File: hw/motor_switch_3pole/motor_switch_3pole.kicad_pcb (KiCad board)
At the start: 2 copper layers, 54 x 54 mm, 24 parts, among them J1 CONN_3X1, J2 CONN_2X1, J3 CONN_6X1, Q1 BSS138, Q2 BSS138

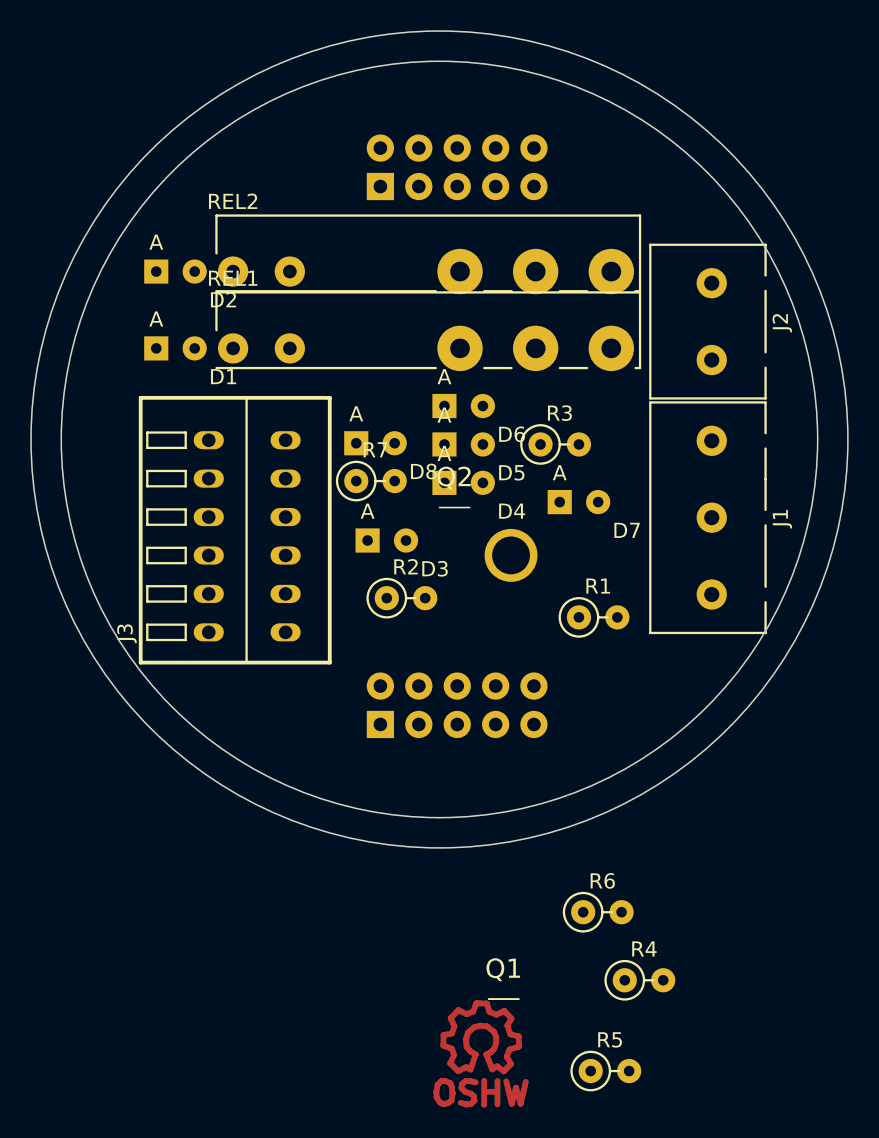
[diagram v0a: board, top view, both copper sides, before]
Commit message: changed to SMD components
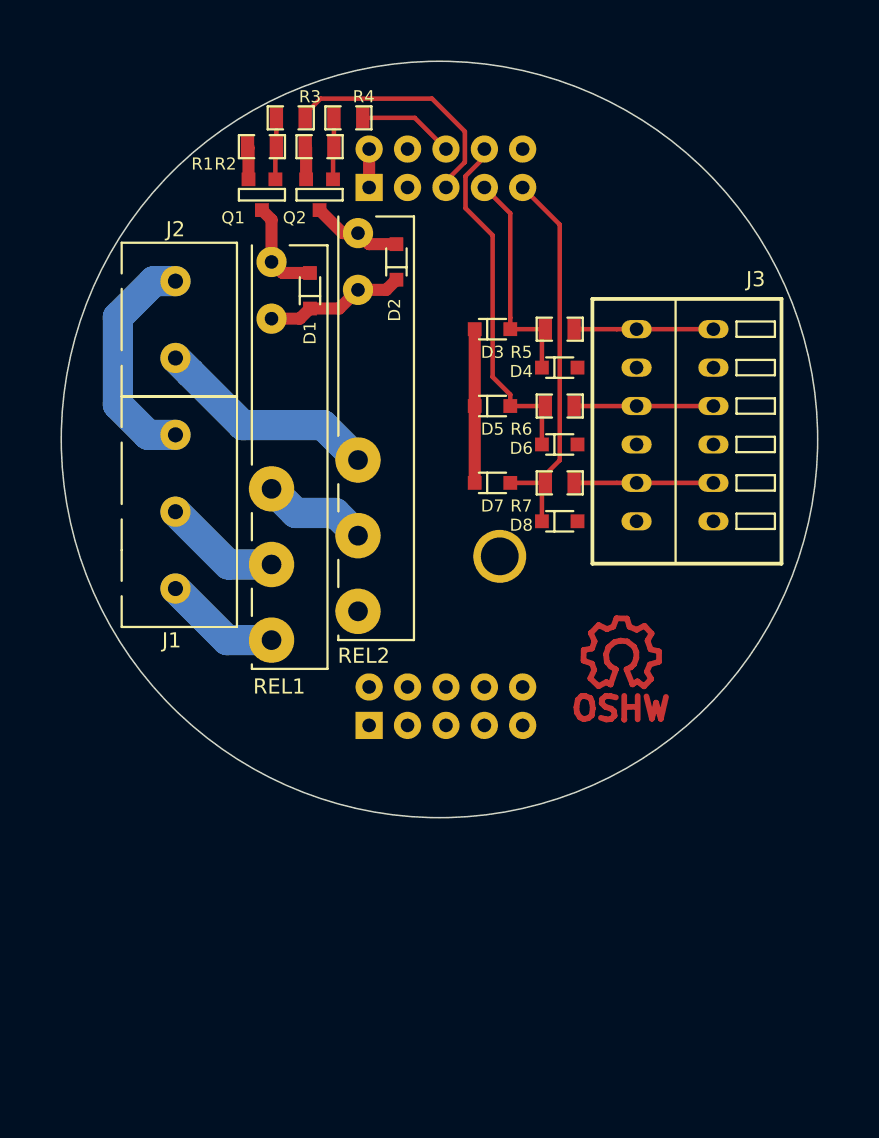
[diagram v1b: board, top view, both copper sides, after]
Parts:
- D1, D2, D3, D4, D5, D6, D7, D8: footprint Diode_THT:D_RM2.54mm -> Diode_SMD:D_SOD323
- R1, R2, R3, R4, R5, R6, R7: footprint Resistor:R_RM2.54mm -> Resistor:R_0805
- moved R4 59.9 mm to (94.0, 78.7)
- moved Q1 55.5 mm to (88.3, 83.8)
- moved R5 49.1 mm to (108.0, 92.7)
- moved J3 38.9 mm to (118.1, 92.7), turned to 270 degrees
- moved R1 37.5 mm to (88.3, 80.6), turned to 180 degrees
- moved J1 37.0 mm to (82.5, 99.7), turned to 270 degrees
- moved J2 35.8 mm to (82.5, 89.5), turned to 270 degrees
- moved R6 33.5 mm to (108.0, 97.8)
- moved R2 30.2 mm to (92.1, 80.6), turned to 180 degrees
- moved R3 27.2 mm to (90.2, 78.7)
- moved LOGO1 27.1 mm to (112.0, 114.3)
- moved Q2 22.5 mm to (92.1, 83.8)
- moved D3 16.2 mm to (103.5, 92.7), turned to 180 degrees
- moved D2 15.9 mm to (97.2, 88.3), turned to 270 degrees
- moved D8 14.4 mm to (108.0, 105.4), turned to 180 degrees
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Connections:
- net Net-(REL1-Pad3) renamed /230V_ON
- D7 pad 1: //button_close -> //switch_close
- D8 pad 2: //button_close -> //switch_close
- J1 pad 1: Net-(J1-Pad1) -> /230V_N
- J1 pad 2: Net-(J1-Pad2) -> /230V_UP
- J1 pad 3: Net-(J1-Pad3) -> /230V_DOWN
- J2 pad 1: Net-(J2-Pad1) -> /230V_N
- J2 pad 2: Net-(J1-Pad2) -> /230V_L
- MOD1 pad 9: (no net) -> //switch_close
- R7 pad 1: //button_close -> //switch_close
- REL1 pad 4: Net-(J1-Pad3) -> /230V_UP
- REL1 pad 5: Net-(J1-Pad1) -> /230V_DOWN
- REL2 pad 3: Net-(J2-Pad1) -> /230V_L
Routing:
- net //switch_close: track 0.00 -> 25.9 mm
- net //button_down: track 0.00 -> 23.7 mm
- net /relay_up_down: track 0.00 -> 16.3 mm
- net /230V_N: track 0.00 -> 15.2 mm
- net //button_up: track 0.00 -> 15.0 mm
- net /230V_L: track 0.00 -> 14.9 mm
- net +5V: track 0.00 -> 10.2 mm
- net +24V: track 0.00 -> 9.32 mm
- net Net-(J3-Pad5): track 0.00 -> 9.21 mm
- net Net-(J3-Pad3): track 0.00 -> 9.21 mm
- net Net-(J3-Pad1): track 0.00 -> 9.21 mm
- net /230V_UP: track 0.00 -> 7.80 mm
- net /230V_DOWN: track 0.00 -> 7.76 mm
- net /230V_ON: track 0.00 -> 7.00 mm
- net GND: track 0.00 -> 6.91 mm
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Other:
- board size 54 x 54 mm -> 50 x 50 mm
- net class 230V added: clearance 1.5, trace_width 2, via_dia 2.5, via_drill 0.8
- net class Default: trace_width 0.25 -> 0.3; via_dia 0.6 -> 0.8
- net class Power added: clearance 0.4, trace_width 0.8, via_dia 1, via_drill 0.5

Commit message: motor control 3pole layouted and ready for review
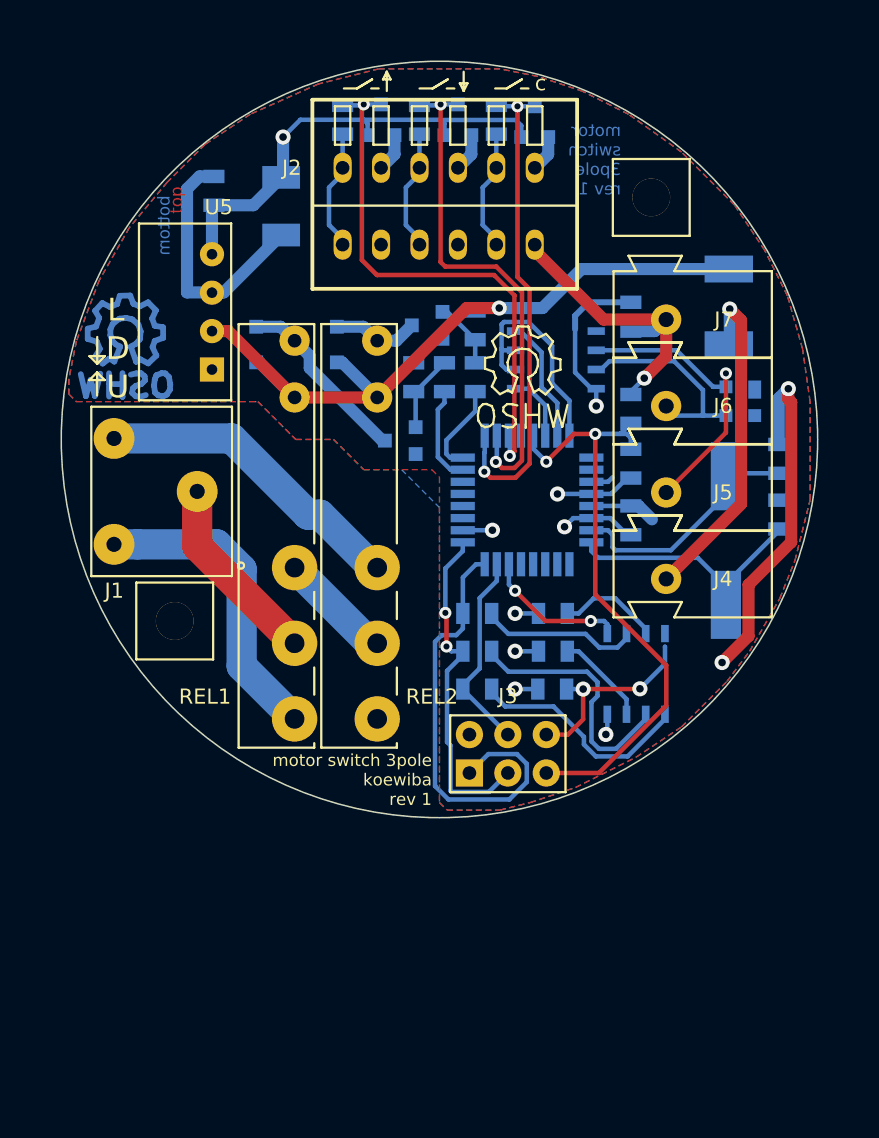
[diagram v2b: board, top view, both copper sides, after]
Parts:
- removed D7, D8: 1N4148, Diode_SMD:D_SOD323
- removed MOD1: bus-module_attiny1634, Modules:bus-module_attiny1634
- added C1: 100nF, Capacitors_SMD:C_0805, B.Cu at (112.6, 105.3)
- added C2: 100nF, Capacitors_SMD:C_0805, B.Cu at (107.5, 116.5)
- added C4: 18pF, Capacitors_SMD:C_0805, B.Cu at (122.4, 101.3)
- added C5: 18pF, Capacitors_SMD:C_0805, B.Cu at (122.4, 105.0)
- added C6: 4,7nF, Capacitors_SMD:C_0805, B.Cu at (112.6, 98.0)
- added C7: 47µF / 4V, Capacitors_SMD:C_0805, B.Cu at (85.1, 83.6)
- added C8: 100nF, Capacitors_SMD:C_0805, B.Cu at (112.6, 91.9)
- added D10: SEMTECH SR05, Diode_SMD:D_SOT143, B.Cu at (119.9, 97.5)
- added F1: FUSE, Resistor:R_1812, B.Cu at (119.1, 91.2)
- added H1: HOLE, Mechanical:HOLE_2.5mm_wo_Copper, F.Cu at (114.0, 84.0)
- added H2: HOLE, Mechanical:HOLE_2.5mm_wo_Copper, F.Cu at (82.5, 112.0)
- added J4: CONN_1, Connector_WAGO:WAGO_243, F.Cu at (111.5, 111.8)
- added J5: CONN_1, Connector_WAGO:WAGO_243, F.Cu at (111.5, 106.0)
- added J6: CONN_1, Connector_WAGO:WAGO_243, F.Cu at (111.5, 100.3)
- added J7: CONN_1, Connector_WAGO:WAGO_243, F.Cu at (111.5, 94.6)
- added LOGO2: Open Hardware, Symbol:Symbol_OSHW-Logo_SilkScreen, F.Cu at (105.5, 95.0)
- added R10: 100, Resistor:R_0805, B.Cu at (102.5, 116.5)
- added R11: 100, Resistor:R_0805, B.Cu at (102.5, 114.0)
- added R12: 10k, Resistor:R_0805, B.Cu at (107.5, 114.0)
- added R13: 10k, Resistor:R_0805, B.Cu at (112.6, 101.6)
- added R8: 10k, Resistor:R_0805, B.Cu at (107.5, 111.5)
- added R9: 100, Resistor:R_0805, B.Cu at (102.5, 111.5)
- added U1: 25LC256, Housings_SOIC:SO8E, B.Cu at (113.0, 115.5)
- added U2: ATMEGA328-TQFP32, Housings_QFP:TQFP-32_7x7mm_Pitch0.8mm, B.Cu at (105.8, 104.0)
- added U3: 7,3728MHz, Crystal:CRY_HC49_SMD, B.Cu at (118.9, 106.7)
- added U4: MAX487ECSA, Housings_SOIC:SO8E, B.Cu at (107.7, 94.7)
- added U5: AM1S-2403, DCDC_Converter:AM1S-XXXX_SIL4, F.Cu at (85.0, 95.4)
- D1, D2, LOGO1, Q1, Q2, R1, R2, R3, R4: moved to B.Cu
- D3: value 1N4148 -> ZD5V6; footprint Diode_SMD:D_SOD323 -> Diode_SMD:D_MINIMELF; moved to B.Cu
- D4, D5, D6: value 1N4148 -> BAT54S; footprint Diode_SMD:D_SOD323 -> Housings_SOT:SOT23-3; moved to B.Cu
- J1: footprint Connector_Miscelleaneus:CLAMP_5,08mm_3pole_stackable -> Connector_WAGO:WAGO_2081-1123
- J2: value CONN_2X1 -> CONN_6X1; footprint Connector_Miscelleaneus:CLAMP_5,08mm_2pole_stackable -> Connector_WAGO:WAGO_233-6
- J3: value CONN_6X1 -> CONN-ISP-6; footprint Connector_Miscelleaneus:WAGO_233-6 -> Connector_Header:HEADER_3x2
- R5, R6, R7: value 1k -> 4k7; moved to B.Cu
- moved LOGO1 39.1 mm to (79.2, 93.0), turned to 180 degrees
- moved J3 33.5 mm to (102.0, 122.0), turned to 0 degrees
- moved R7 24.4 mm to (103.8, 78.9), turned to 270 degrees
- moved D6 21.4 mm to (106.3, 79.0), turned to 0 degrees
- moved R6 21.1 mm to (98.7, 78.9), turned to 270 degrees
- moved D4 20.2 mm to (96.1, 78.9), turned to 0 degrees
- moved R5 19.9 mm to (93.6, 78.9), turned to 270 degrees
- moved R3 19.9 mm to (100.3, 95.9), turned to 270 degrees
- moved R4 19.1 mm to (102.4, 95.9), turned to 270 degrees
- moved D5 19.1 mm to (101.2, 78.9), turned to 0 degrees
- moved Q1 18.7 mm to (97.4, 100.1), turned to 90 degrees
- moved R1 18.2 mm to (98.3, 95.9), turned to 90 degrees
- moved D3 16.2 mm to (89.5, 84.6), turned to 90 degrees
- moved R2 15.7 mm to (102.4, 92.5), turned to 90 degrees
- moved J2 13.4 mm to (93.6, 82.0), turned to 0 degrees
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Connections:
- D3 pad 1: //button_up -> GND
- D4 pad 2: //button_up -> +5V
- D5 pad 1: //button_down -> GND
- D6 pad 2: //button_down -> +5V
- J1 pad 1: /230V_N -> /230V_UP
- J1 pad 2: /230V_UP -> /230V_DOWN
- J1 pad 3: /230V_DOWN -> /230V_L
- J2 pad 1: /230V_N -> Net-(J2-Pad1)
- J2 pad 2: /230V_L -> GND
- J3 pad 1: Net-(J3-Pad1) -> /bus_atmega328_basic/PB4_MISO
- J3 pad 2: GND -> +5V
- J3 pad 3: Net-(J3-Pad3) -> /bus_atmega328_basic/PB5_SCK
- J3 pad 4: GND -> /bus_atmega328_basic/PB3_MOSI
- J3 pad 5: Net-(J3-Pad5) -> /bus_atmega328_basic//RESET
- R5 pad 2: Net-(J3-Pad1) -> Net-(J2-Pad1)
- R6 pad 2: Net-(J3-Pad3) -> Net-(J2-Pad3)
- R7 pad 2: Net-(J3-Pad5) -> Net-(J2-Pad5)
- REL1 pad 4: /230V_UP -> /230V_DOWN
- REL1 pad 5: /230V_DOWN -> /230V_UP
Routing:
- net GND: track 6.91 -> 87.7 mm, vias 0 -> 5
- net +5V: track 10.2 -> 59.7 mm, vias 0 -> 9
- net /bus_atmega328_basic//RESET: track 0.00 -> 40.0 mm, vias 0 -> 2
- net +24V: track 9.32 -> 46.7 mm, vias 0 -> 1
- net /bus_atmega328_basic/PB4_MISO: track 0.00 -> 29.6 mm
- net /bus_atmega328_basic/PB5_SCK: track 0.00 -> 22.7 mm, vias 0 -> 2
- net Net-(F1-Pad2): track 0.00 -> 22.6 mm, vias 0 -> 1
- net //button_up: track 15.0 -> 36.1 mm, vias 0 -> 2
- net /bus_atmega328_basic/A: track 0.00 -> 19.8 mm, vias 0 -> 1
- net Net-(C5-Pad1): track 0.00 -> 18.8 mm
- net Net-(C4-Pad1): track 0.00 -> 17.7 mm
- net /bus_atmega328_basic/SCK: track 0.00 -> 17.0 mm
- net /bus_atmega328_basic/TXD0EN: track 0.00 -> 15.3 mm
- net /230V_N: track 15.2 -> 0.00 mm
- net /bus_atmega328_basic/MOSI: track 0.00 -> 15.1 mm
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- added copper zone on F.Cu, net +5V
- added copper zone on B.Cu, net GND
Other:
- net class 230V: clearance 1.5 -> 1
- net class Power: clearance 0.4 -> 0.2
- board text added: "D"
- board text added: "L"
- board text added: "U"
- board text added: "bottom"
- board text added: "c"
- board text added: "motor switch 3pole koewiba rev 1"
- board text added: "motor switch 3pole rev 1"
- board text added: "top"

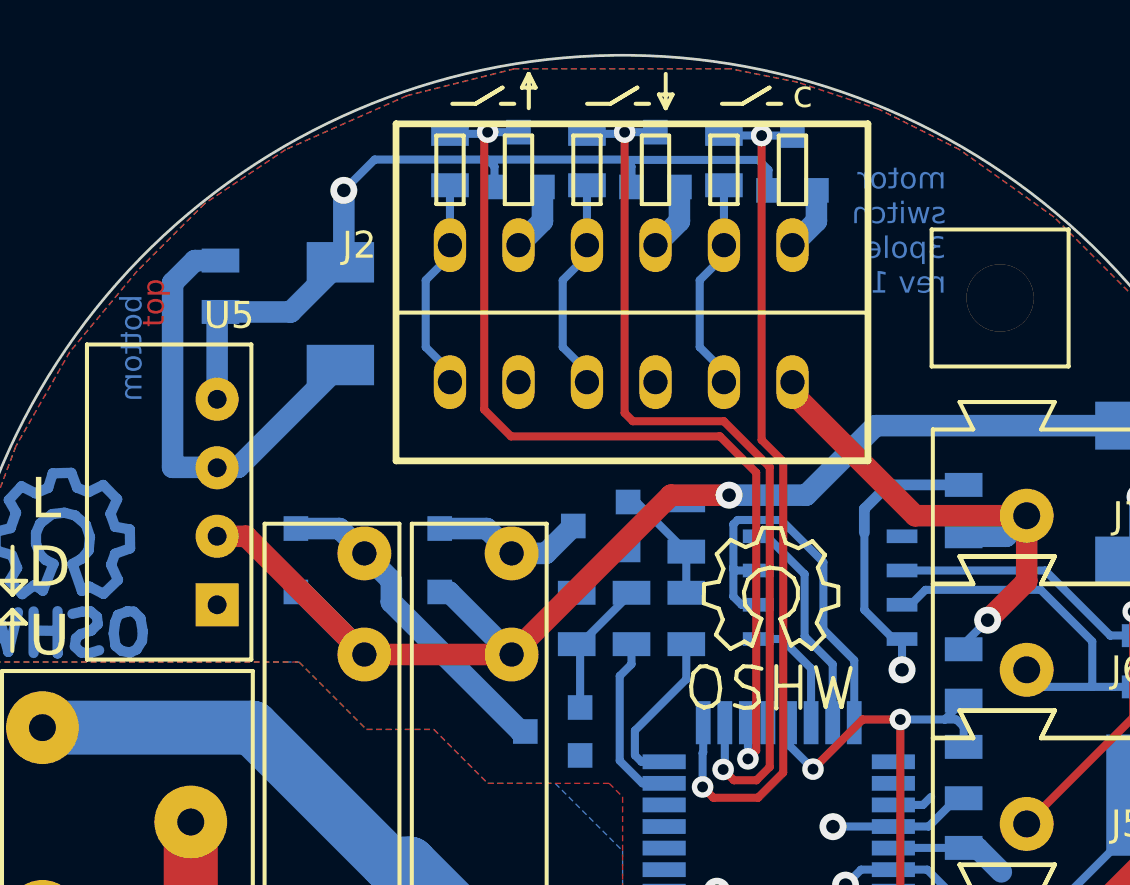
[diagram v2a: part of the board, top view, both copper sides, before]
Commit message: Final revision 1 files of motor_switch_3pole added. Prototype PCBs of this revision have been ordered
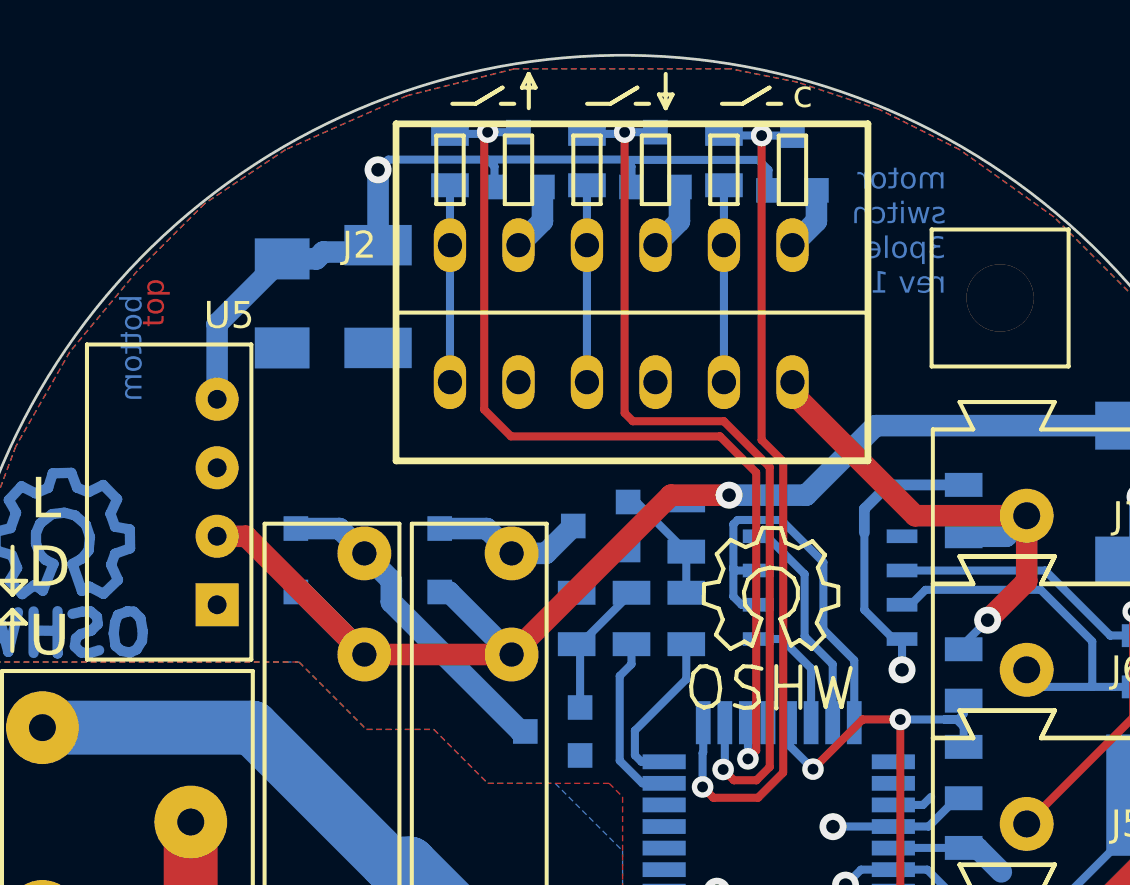
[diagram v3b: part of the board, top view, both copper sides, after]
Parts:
- C7: value 47µF / 4V -> 100µF / 6V; footprint Capacitors_SMD:C_0805 -> Capacitors_SMD:C_1206
- J1: value CONN_3X1 -> WAGO 2081-1123
- J2: value CONN_6X1 -> WAGO 233-506
- J4: value CONN_1 -> WAGO 243-723
- J5: value CONN_1 -> WAGO 243-724
- J6: value CONN_1 -> WAGO 243-721
- J7: value CONN_1 -> WAGO 243-722
- REL1, REL2: value FINDER_36.11-4001 -> FINDER_34.51.7.024
- U5: value AM1S-2403 -> AM1S-2405
- moved C7 2.37 mm to (87.4, 84.2), turned to 270 degrees
- moved D3 1.53 mm to (90.9, 83.9)
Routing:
- net GND: track 87.7 -> 71.0 mm
- net Net-(J2-Pad5): track 8.37 -> 7.62 mm
- net Net-(J2-Pad3): track 8.50 -> 7.75 mm
- net Net-(J2-Pad1): track 8.55 -> 7.80 mm
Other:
- net class Power: trace_width 0.8 -> 0.3
